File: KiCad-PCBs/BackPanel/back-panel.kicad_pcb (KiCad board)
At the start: 2 copper layers, 93.3 x 69.3 mm, 12 parts, among them J14 Pwr Pins

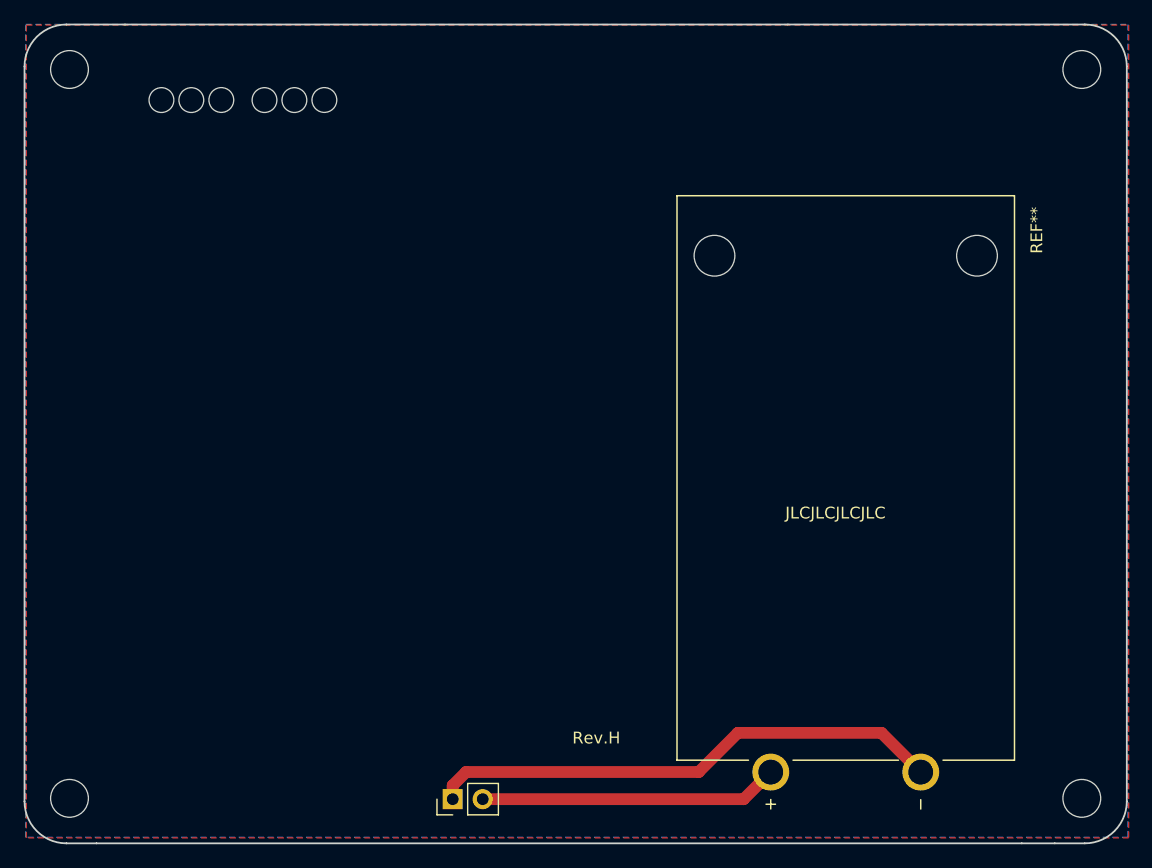
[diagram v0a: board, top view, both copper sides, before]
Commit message: Improving Battery Holder Footprint, adding polarity marks, going back from Rev.H to Rev.C (do not sync Revs)
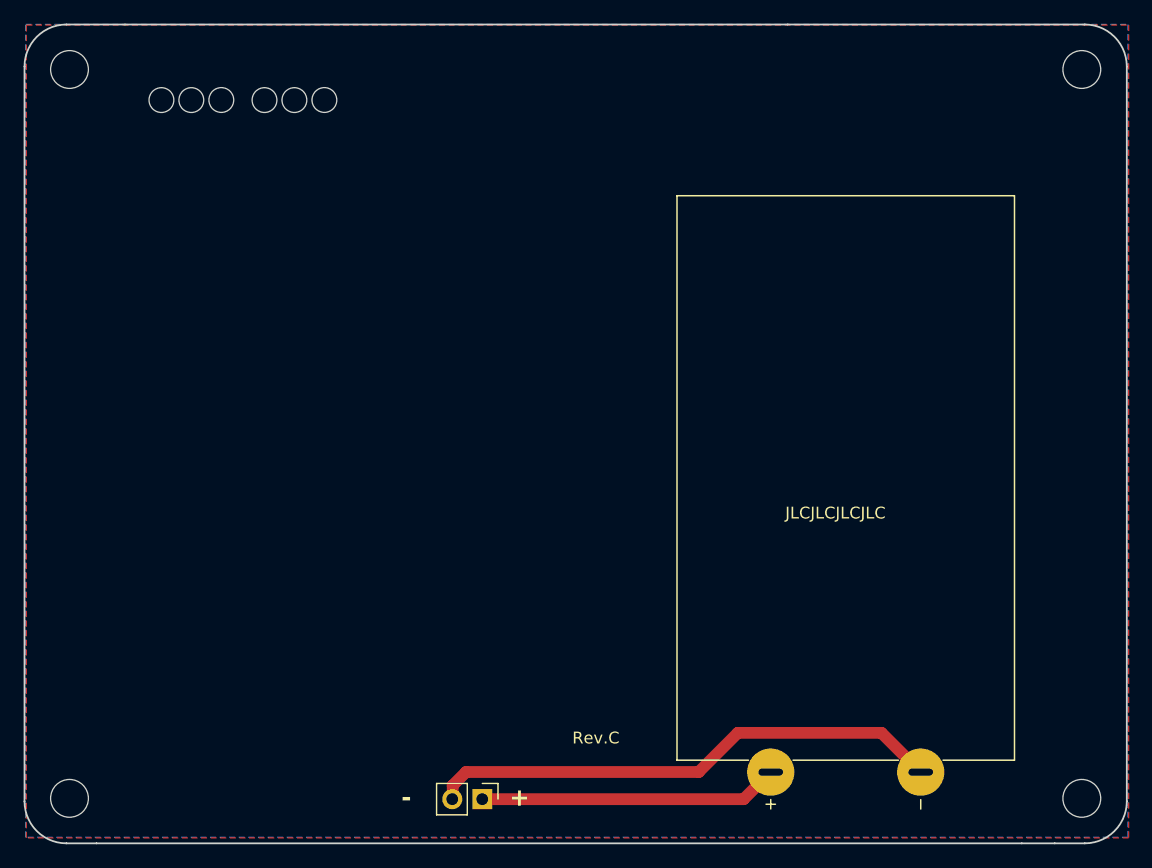
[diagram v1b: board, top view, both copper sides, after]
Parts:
- moved J14 2.50 mm to (134.6, 125.5), turned to -90 degrees
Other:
- board text added: "Rev.C"
- board text removed: "Rev.H"
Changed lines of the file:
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@@
 			(drillshape 0)
 			(scaleselection 1)
-			(outputdirectory "gerber")
+			(outputdirectory "gerber/")
 		)
 	)
@@
 	(footprint "Connector_PinHeader_2.54mm:PinHeader_1x02_P2.54mm_Vertical"
 		(layer "F.Cu")
-		(at 132.115 125.5 90)
+		(at 134.62 125.5 -90)
 		(descr "Through hole straight pin header, 1x02, 2.54mm pitch, single row")
 		(tags "Through hole pin header THT 1x02 2.54mm single row")
 		(property "Reference" "J14"
-			(at 0 -2.33 -90)
+			(at 0 -2.33 90)
 			(layer "F.SilkS")
 			(hide yes)
@@
 		)
 		(property "Value" "Pwr Pins"
-			(at 0 4.87 -90)
+			(at 0 4.87 90)
 			(layer "F.Fab")
 			(effects
@@
 		)
 		(property "Footprint" "Connector_PinHeader_2.54mm:PinHeader_1x02_P2.54mm_Vertical"
-			(at 0 0 90)
+			(at 0 0 -90)
 			(unlocked yes)
 			(layer "F.Fab")
@@
 		)
 		(property "Datasheet" ""
-			(at 0 0 90)
+			(at 0 0 -90)
 			(unlocked yes)
 			(layer "F.Fab")
@@
 		)
 		(property "Description" "Generic connector, single row, 01x02, script generated"
-			(at 0 0 90)
+			(at 0 0 -90)
 			(unlocked yes)
 			(layer "F.Fab")
@@
 		)
 		(attr through_hole)
+		(fp_line
+			(start -1.33 3.87)
+			(end 1.33 3.87)
+			(stroke
+				(width 0.12)
+				(type solid)
+			)
+			(layer "F.SilkS")
+		)
+		(fp_line
+			(start -1.33 1.27)
+			(end -1.33 3.87)
+			(stroke
+				(width 0.12)
+				(type solid)
+			)
+			(layer "F.SilkS")
+		)
+		(fp_line
+			(start -1.33 1.27)
+			(end 1.33 1.27)
+			(stroke
+				(width 0.12)
+				(type solid)
+			)
+			(layer "F.SilkS")
+		)
+		(fp_line
+			(start 1.33 1.27)
+			(end 1.33 3.87)
+			(stroke
+				(width 0.12)
+				(type solid)
+			)
+			(layer "F.SilkS")
+		)
+		(fp_line
+			(start -1.33 0)
+			(end -1.33 -1.33)
+			(stroke
+				(width 0.12)
+				(type solid)
+			)
+			(layer "F.SilkS")
+		)
 		(fp_line
 			(start -1.33 -1.33)
@@
 		)
 		(fp_line
-			(start -1.33 0)
-			(end -1.33 -1.33)
-			(stroke
-				(width 0.12)
-				(type solid)
-			)
-			(layer "F.SilkS")
-		)
-		(fp_line
-			(start 1.33 1.27)
-			(end 1.33 3.87)
-			(stroke
-				(width 0.12)
-				(type solid)
-			)
-			(layer "F.SilkS")
-		)
-		(fp_line
-			(start -1.33 1.27)
-			(end 1.33 1.27)
-			(stroke
-				(width 0.12)
-				(type solid)
-			)
-			(layer "F.SilkS")
-		)
-		(fp_line
-			(start -1.33 1.27)
-			(end -1.33 3.87)
-			(stroke
-				(width 0.12)
-				(type solid)
-			)
-			(layer "F.SilkS")
-		)
-		(fp_line
-			(start -1.33 3.87)
-			(end 1.33 3.87)
-			(stroke
-				(width 0.12)
-				(type solid)
-			)
-			(layer "F.SilkS")
+			(start -1.8 4.35)
+			(end 1.8 4.35)
+			(stroke
+				(width 0.05)
+				(type solid)
+			)
+			(layer "F.CrtYd")
+		)
+		(fp_line
+			(start 1.8 4.35)
+			(end 1.8 -1.8)
+			(stroke
+				(width 0.05)
+				(type solid)
+			)
+			(layer "F.CrtYd")
+		)
+		(fp_line
+			(start -1.8 -1.8)
+			(end -1.8 4.35)
+			(stroke
+				(width 0.05)
+				(type solid)
+			)
+			(layer "F.CrtYd")
 		)
 		(fp_line
@@
 		)
 		(fp_line
-			(start -1.8 -1.8)
-			(end -1.8 4.35)
-			(stroke
-				(width 0.05)
-				(type solid)
-			)
-			(layer "F.CrtYd")
-		)
-		(fp_line
-			(start 1.8 4.35)
-			(end 1.8 -1.8)
-			(stroke
-				(width 0.05)
-				(type solid)
-			)
-			(layer "F.CrtYd")
-		)
-		(fp_line
-			(start -1.8 4.35)
-			(end 1.8 4.35)
-			(stroke
-				(width 0.05)
-				(type solid)
-			)
-			(layer "F.CrtYd")
+			(start -1.27 3.81)
+			(end -1.27 -0.635)
+			(stroke
+				(width 0.1)
+				(type solid)
+			)
+			(layer "F.Fab")
+		)
+		(fp_line
+			(start 1.27 3.81)
+			(end -1.27 3.81)
+			(stroke
+				(width 0.1)
+				(type solid)
+			)
+			(layer "F.Fab")
+		)
+		(fp_line
+			(start -1.27 -0.635)
+			(end -0.635 -1.27)
+			(stroke
+				(width 0.1)
+				(type solid)
+			)
+			(layer "F.Fab")
+		)
+		(fp_line
+			(start -0.635 -1.27)
+			(end 1.27 -1.27)
+			(stroke
+				(width 0.1)
+				(type solid)
+			)
+			(layer "F.Fab")
 		)
 		(fp_line
@@
 			(layer "F.Fab")
 		)
-		(fp_line
-			(start -0.635 -1.27)
-			(end 1.27 -1.27)
-			(stroke
-				(width 0.1)
-				(type solid)
-			)
-			(layer "F.Fab")
-		)
-		(fp_line
-			(start -1.27 -0.635)
-			(end -0.635 -1.27)
-			(stroke
-				(width 0.1)
-				(type solid)
-			)
-			(layer "F.Fab")
-		)
-		(fp_line
-			(start 1.27 3.81)
-			(end -1.27 3.81)
-			(stroke
-				(width 0.1)
-				(type solid)
-			)
-			(layer "F.Fab")
-		)
-		(fp_line
-			(start -1.27 3.81)
-			(end -1.27 -0.635)
-			(stroke
-				(width 0.1)
-				(type solid)
-			)
-			(layer "F.Fab")
-		)
 		(fp_text user "${REFERENCE}"
-			(at 0 1.27 0)
+			(at 0 1.27 180)
 			(layer "F.Fab")
 			(effects
@@
 		)
 		(pad "1" thru_hole rect
-			(at 0 0 90)
+			(at 0 0 270)
 			(size 1.7 1.7)
 			(drill 1)
@@
 		)
 		(pad "2" thru_hole oval
-			(at 0 2.54 90)
+			(at 0 2.54 270)
 			(size 1.7 1.7)
 			(drill 1)
@@
 		(at 165.4 98.3 -90)
 		(property "Reference" "REF**"
-			(at -20.975 -16.175 -90)
-			(layer "F.SilkS")
+			(at -20.975 -16.175 270)
+			(layer "F.SilkS")
+			(hide yes)
 			(effects
 				(font
@@
 			(layer "F.Fab")
 		)
-		(pad "" np_thru_hole circle
-			(at -18.82 -11.115 270)
-			(size 3.45 3.45)
-			(drill 3.45)
-			(layers "*.Cu" "*.Mask")
-		)
-		(pad "" np_thru_hole circle
-			(at -18.82 11.115 270)
-			(size 3.45 3.45)
-			(drill 3.45)
-			(layers "*.Cu" "*.Mask")
-		)
 		(pad "N" thru_hole circle
 			(at 24.91 -6.35 270)
-			(size 3.126 3.126)
-			(drill 2.11)
+			(size 4 4)
+			(drill oval 0.6 2.1)
 			(layers "*.Cu" "*.Mask")
 			(remove_unused_layers no)
@@
 		(pad "P" thru_hole circle
 			(at 24.91 6.35 270)
-			(size 3.126 3.126)
-			(drill 2.11)
+			(size 4 4)
+			(drill oval 0.6 2.1)
 			(layers "*.Cu" "*.Mask")
 			(remove_unused_layers no)
@@
 		)
 	)
+	(gr_text "-"
+		(at 127.762 126.238 0)
+		(layer "F.SilkS")
+		(effects
+			(font
+				(size 1.5 1.5)
+				(thickness 0.3)
+				(bold yes)
+			)
+			(justify left bottom)
+		)
+	)
 	(gr_text "JLCJLCJLCJLC"
 		(at 160.274 101.854 -0)
@@
 		)
 	)
-	(gr_text "Rev.H"
+	(gr_text "+"
+		(at 136.906 126.238 0)
+		(layer "F.SilkS")
+		(effects
+			(font
+				(size 1.5 1.5)
+				(thickness 0.3)
+				(bold yes)
+			)
+			(justify left bottom)
+		)
+	)
+	(gr_text "Rev.C"
 		(at 142.24 120.904 0)
 		(layer "F.SilkS")
